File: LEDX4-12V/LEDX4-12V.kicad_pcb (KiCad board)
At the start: 2 copper layers, 22 parts, among them K1001 CONN_2, K1002 CONN_2

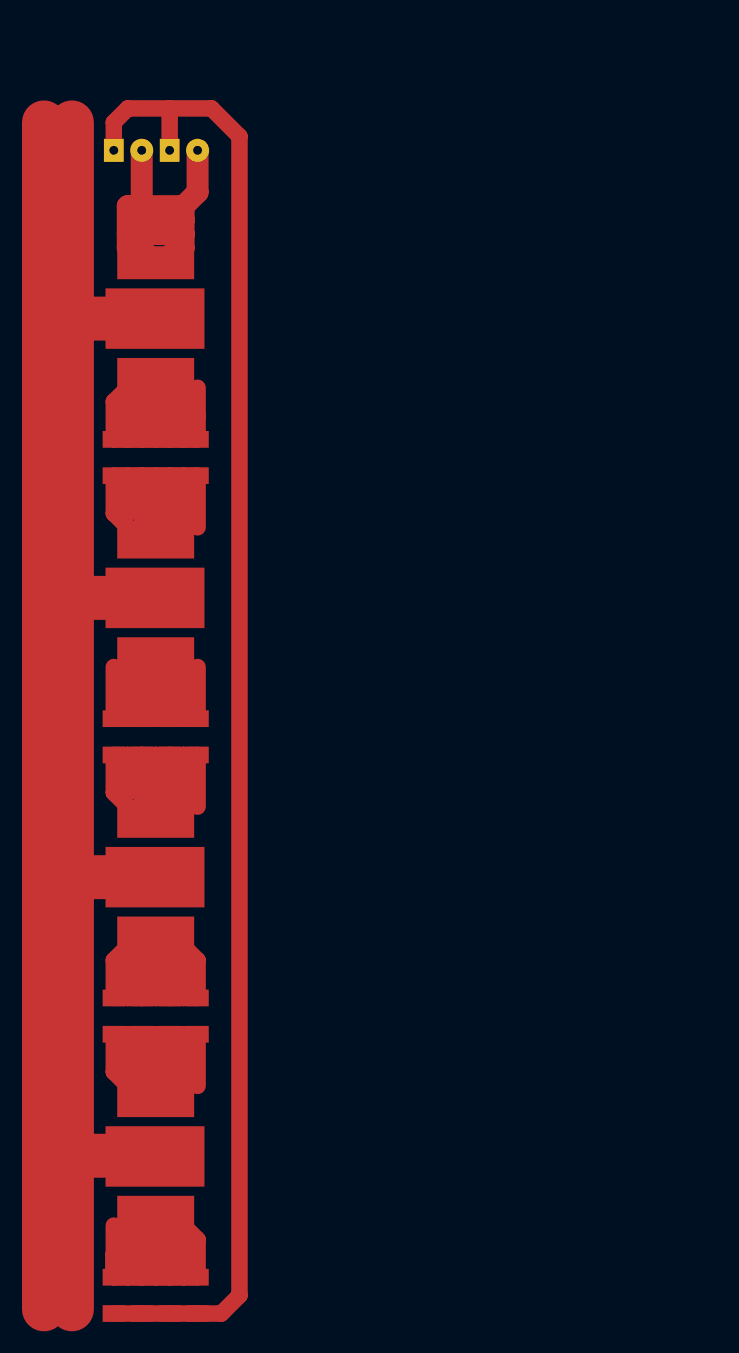
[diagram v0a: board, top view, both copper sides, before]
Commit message: UPDATE LED 4x
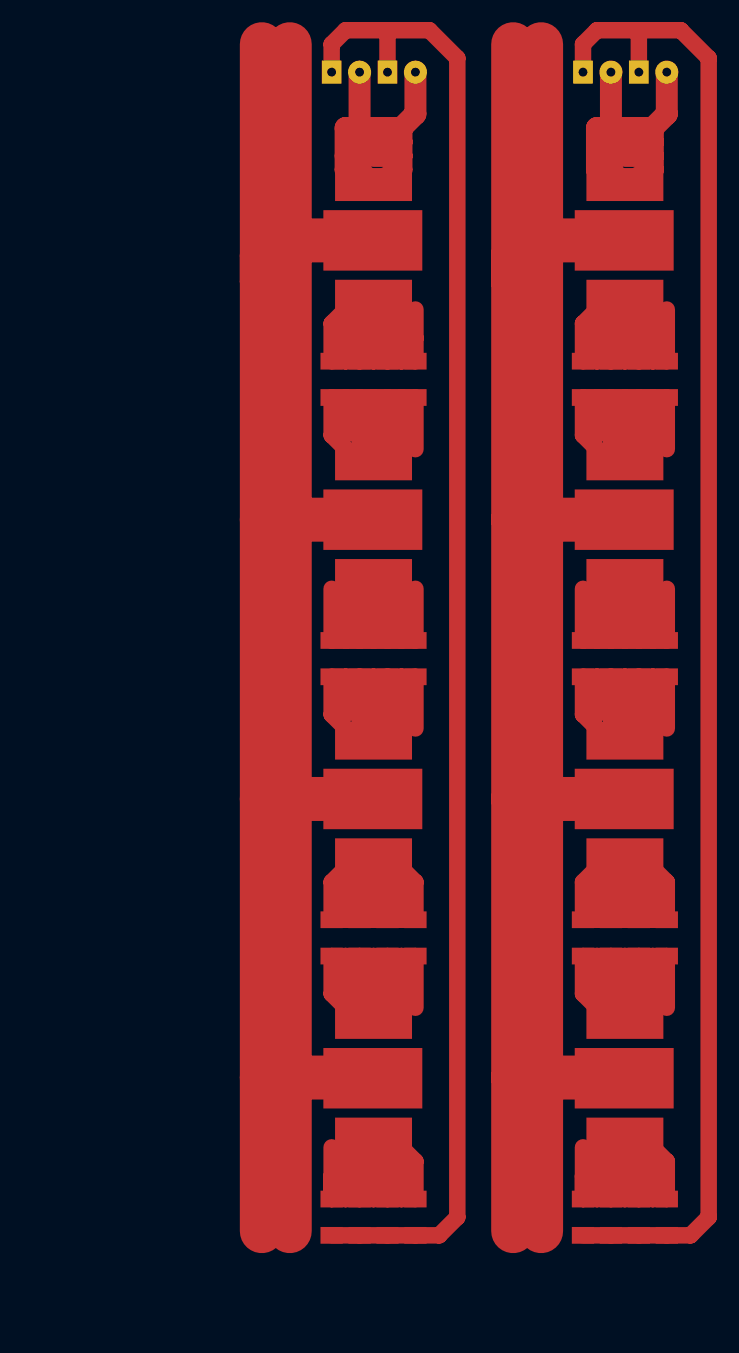
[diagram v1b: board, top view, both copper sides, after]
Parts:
- added D1001: LED, LED-CMS-1W, F.Cu at (70.6, 60.2)
- added D1002: LED, LED-CMS-1W, F.Cu at (70.6, 85.6)
- added D1003: LED, LED-CMS-1W, F.Cu at (70.6, 111.0)
- added D1004: LED, LED-CMS-1W, F.Cu at (70.6, 136.4)
- added K1001: CONN_2, KK-2, B.Cu at (74.4, 45.0)
- added K1002: CONN_2, KK-2, B.Cu at (69.3, 45.0)
- added R1001: R, SM1206, F.Cu at (69.3, 72.9)
- added R1002: R, SM1206, F.Cu at (71.9, 98.3)
- added R1003: R, SM1206, F.Cu at (74.4, 123.7)
- added R1004: R, SM1206, F.Cu at (69.3, 149.1)
- added R1005: R, SM1206, F.Cu at (66.8, 72.9)
- added R1006: R, SM1206, F.Cu at (71.9, 72.9)
- added R1007: R, SM1206, F.Cu at (74.4, 72.9)
- added R1008: R, SM1206, F.Cu at (69.3, 98.3)
- added R1009: R, SM1206, F.Cu at (74.4, 98.3)
- added R1010: R, SM1206, F.Cu at (66.8, 98.3)
- added R1011: R, SM1206, F.Cu at (71.9, 123.7)
- added R1012: R, SM1206, F.Cu at (69.3, 123.7)
- added R1013: R, SM1206, F.Cu at (66.8, 123.7)
- added R1014: R, SM1206, F.Cu at (71.9, 149.1)
- added R1015: R, SM1206, F.Cu at (66.8, 149.1)
- added R1016: R, SM1206, F.Cu at (74.4, 149.1)
- moved R1005 21.0 mm to (43.9, 72.9)
- moved R1013 21.0 mm to (43.9, 123.7)
- moved D1001 21.0 mm to (47.8, 60.2)
- moved D1002 21.0 mm to (47.8, 85.6)
- moved D1003 21.0 mm to (47.8, 111.0)
- moved D1004 21.0 mm to (47.8, 136.4)
- moved R1001 21.0 mm to (46.5, 72.9)
- moved R1003 21.0 mm to (51.6, 123.7)
- moved R1006 21.0 mm to (49.0, 72.9)
- moved R1007 21.0 mm to (51.6, 72.9)
- moved R1010 21.0 mm to (43.9, 98.3)
- moved R1011 21.0 mm to (49.0, 123.7)
- moved R1012 21.0 mm to (46.5, 123.7)
- moved R1015 21.0 mm to (43.9, 149.1)
- moved K1001 21.0 mm to (51.6, 45.0)
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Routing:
- net GND: track 303.3 -> 606.7 mm
- net N-000008: track 136.9 -> 273.8 mm
- net N-000005: track 67.8 -> 135.5 mm
- net N-000007: track 56.9 -> 113.9 mm
- net N-000003: track 54.4 -> 108.9 mm
- net N-000006: track 54.2 -> 108.4 mm
- net N-000002: track 50.8 -> 101.6 mm
- net N-000004: track 50.8 -> 101.6 mm
- net N-000001: track 50.6 -> 101.1 mm
